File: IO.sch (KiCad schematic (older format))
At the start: 16 parts, among them U3 74AC541, U4 74LS138, U5 74HC245, U7 74LS148

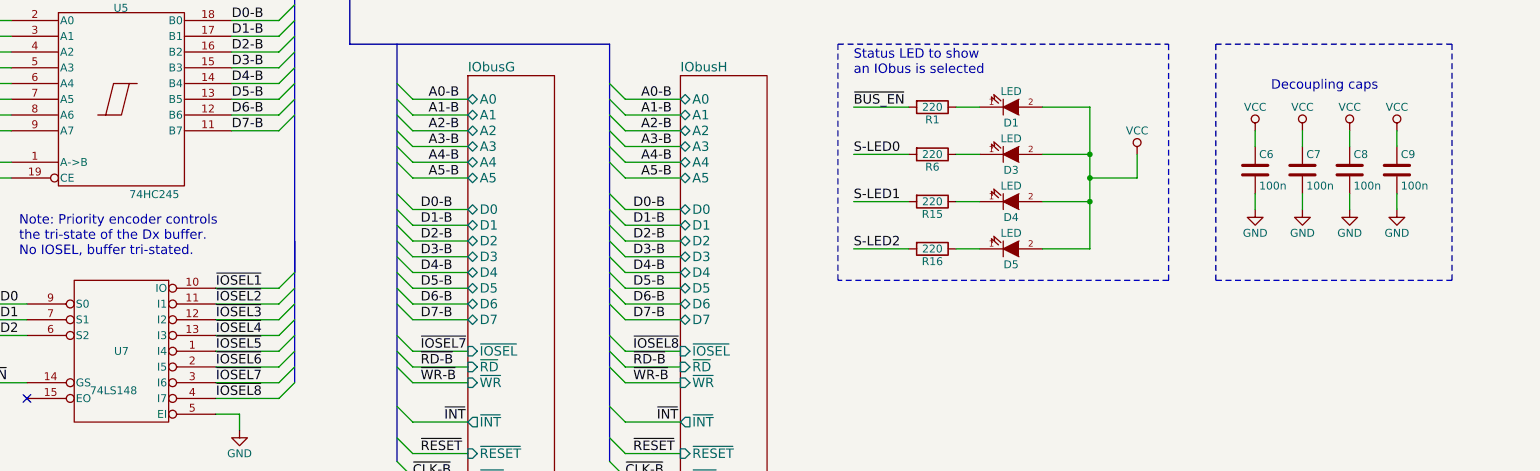
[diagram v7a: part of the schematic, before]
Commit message: Update PCB, better layout. Got Addr bus back in order
Think having both USB and DC input would be useful. Switchmode a plus
then plugpack/battery etc voltage doesn't matter. Plus I have a bag full
of those parts too!

I've refdes'd the linear reg just to deal with the net. Will remove if
we both are happy with switcher. Linear cheaper to kit out I guess.

Was trying to find a better way to combine USB and DC power rails than
just schottky diodes. If you have any ideas.

Going to have a big area under the IO ports, might be worth adding a USB
to serial, or sacrifice a IO port for some blinky LEDs and buttons?
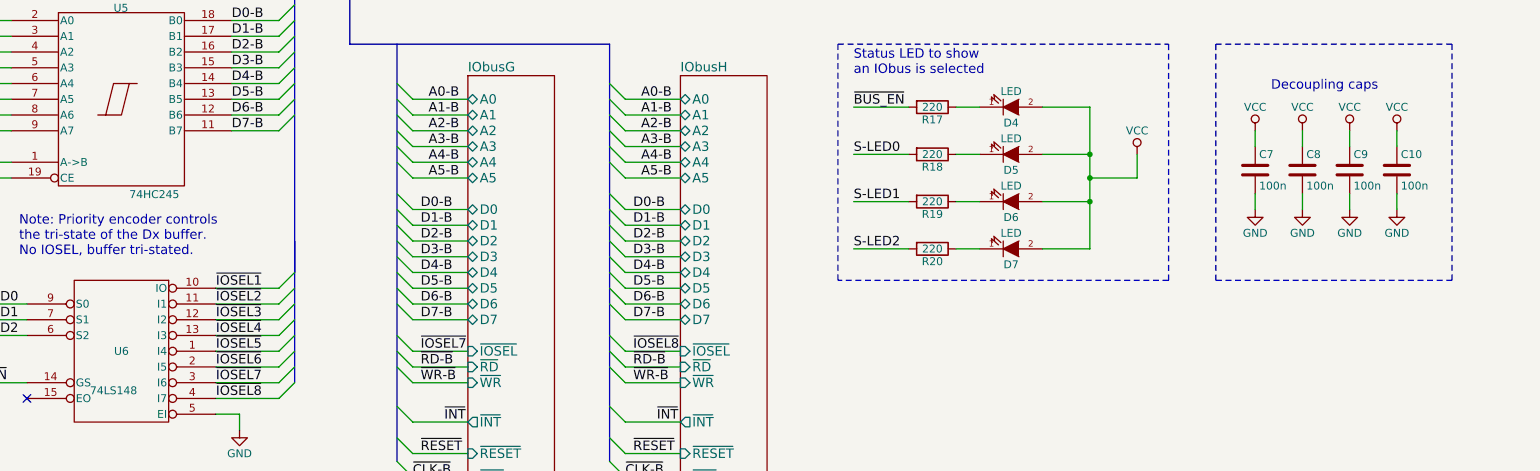
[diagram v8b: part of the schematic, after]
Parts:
- renumbered C9 to C10, C6 to C7, C7 to C8, C8 to C9, D1 to D4, D3 to D5, D4 to D6, D5 to D7, R1 to R17, R6 to R18, R15 to R19, R16 to R20, U7 to U6
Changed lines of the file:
@@
 $EndSheet
 $Comp
-L GND #PWR018
+L GND #PWR029
 U 1 1 5780EA7D
 P 1500 2000
-F 0 "#PWR018" H 1500 1750 50  0001 C CNN
+F 0 "#PWR029" H 1500 1750 50  0001 C CNN
 F 1 "GND" H 1500 1850 50  0000 C CNN
 F 2 "" H 1500 2000 50  0000 C CNN
@@
 	3250 3300 3350 3200
 $Comp
-L C C6
+L C C7
 U 1 1 57887A68
 P 9450 5150
-F 0 "C6" H 9475 5250 50  0000 L CNN
+F 0 "C7" H 9475 5250 50  0000 L CNN
 F 1 "100n" H 9475 5050 50  0000 L CNN
 F 2 "Capacitors_SMD:C_0805_HandSoldering" H 9488 5000 50  0001 C CNN
@@
 $EndComp
 $Comp
-L GND #PWR019
+L GND #PWR030
 U 1 1 57887A6E
 P 9450 5400
-F 0 "#PWR019" H 9450 5150 50  0001 C CNN
+F 0 "#PWR030" H 9450 5150 50  0001 C CNN
 F 1 "GND" H 9450 5250 50  0000 C CNN
 F 2 "" H 9450 5400 50  0000 C CNN
@@
 $EndComp
 $Comp
-L VCC #PWR020
+L VCC #PWR031
 U 1 1 57887A74
 P 9450 4900
-F 0 "#PWR020" H 9450 4750 50  0001 C CNN
+F 0 "#PWR031" H 9450 4750 50  0001 C CNN
 F 1 "VCC" H 9450 5050 50  0000 C CNN
 F 2 "" H 9450 4900 50  0000 C CNN
@@
 $EndComp
 $Comp
-L C C7
+L C C8
 U 1 1 57887A7C
 P 9750 5150
-F 0 "C7" H 9775 5250 50  0000 L CNN
+F 0 "C8" H 9775 5250 50  0000 L CNN
 F 1 "100n" H 9775 5050 50  0000 L CNN
 F 2 "Capacitors_SMD:C_0805_HandSoldering" H 9788 5000 50  0001 C CNN
@@
 $EndComp
 $Comp
-L GND #PWR021
+L GND #PWR032
 U 1 1 57887A82
 P 9750 5400
-F 0 "#PWR021" H 9750 5150 50  0001 C CNN
+F 0 "#PWR032" H 9750 5150 50  0001 C CNN
 F 1 "GND" H 9750 5250 50  0000 C CNN
 F 2 "" H 9750 5400 50  0000 C CNN
@@
 $EndComp
 $Comp
-L VCC #PWR022
+L VCC #PWR033
 U 1 1 57887A88
 P 9750 4900
-F 0 "#PWR022" H 9750 4750 50  0001 C CNN
+F 0 "#PWR033" H 9750 4750 50  0001 C CNN
 F 1 "VCC" H 9750 5050 50  0000 C CNN
 F 2 "" H 9750 4900 50  0000 C CNN
@@
 	3250 3800 3350 3700
 $Comp
-L C C8
+L C C9
 U 1 1 5785CC55
 P 10050 5150
-F 0 "C8" H 10075 5250 50  0000 L CNN
+F 0 "C9" H 10075 5250 50  0000 L CNN
 F 1 "100n" H 10075 5050 50  0000 L CNN
 F 2 "Capacitors_SMD:C_0805_HandSoldering" H 10088 5000 50  0001 C CNN
@@
 $EndComp
 $Comp
-L GND #PWR023
+L GND #PWR034
 U 1 1 5785CC5B
 P 10050 5400
-F 0 "#PWR023" H 10050 5150 50  0001 C CNN
+F 0 "#PWR034" H 10050 5150 50  0001 C CNN
 F 1 "GND" H 10050 5250 50  0000 C CNN
 F 2 "" H 10050 5400 50  0000 C CNN
@@
 $EndComp
 $Comp
-L VCC #PWR024
+L VCC #PWR035
 U 1 1 5785CC61
 P 10050 4900
-F 0 "#PWR024" H 10050 4750 50  0001 C CNN
+F 0 "#PWR035" H 10050 4750 50  0001 C CNN
 F 1 "VCC" H 10050 5050 50  0000 C CNN
 F 2 "" H 10050 4900 50  0000 C CNN
@@
 ~IOSEL8
 $Comp
-L C C9
+L C C10
 U 1 1 57897A03
 P 10350 5150
-F 0 "C9" H 10375 5250 50  0000 L CNN
+F 0 "C10" H 10375 5250 50  0000 L CNN
 F 1 "100n" H 10375 5050 50  0000 L CNN
 F 2 "Capacitors_SMD:C_0805_HandSoldering" H 10388 5000 50  0001 C CNN
@@
 $EndComp
 $Comp
-L GND #PWR025
+L GND #PWR036
 U 1 1 57897A09
 P 10350 5400
-F 0 "#PWR025" H 10350 5150 50  0001 C CNN
+F 0 "#PWR036" H 10350 5150 50  0001 C CNN
 F 1 "GND" H 10350 5250 50  0000 C CNN
 F 2 "" H 10350 5400 50  0000 C CNN
@@
 $EndComp
 $Comp
-L VCC #PWR026
+L VCC #PWR037
 U 1 1 57897A0F
 P 10350 4900
-F 0 "#PWR026" H 10350 4750 50  0001 C CNN
+F 0 "#PWR037" H 10350 4750 50  0001 C CNN
 F 1 "VCC" H 10350 5050 50  0000 C CNN
 F 2 "" H 10350 4900 50  0000 C CNN
@@
 ~RESET
 $Comp
-L 74LS148 U7
+L 74LS148 U6
 U 1 1 5790D09E
 P 2250 6300
-F 0 "U7" H 2250 6300 50  0000 C CNN
+F 0 "U6" H 2250 6300 50  0000 C CNN
 F 1 "74LS148" H 2300 6050 50  0000 C CNN
 F 2 "Housings_DIP:DIP-16_W7.62mm_LongPads" H 2250 6300 50  0001 C CNN
@@
 $EndComp
 $Comp
-L GND #PWR027
+L GND #PWR038
 U 1 1 5790EE64
 P 3000 6800
-F 0 "#PWR027" H 3000 6550 50  0001 C CNN
+F 0 "#PWR038" H 3000 6550 50  0001 C CNN
 F 1 "GND" H 3000 6650 50  0000 C CNN
 F 2 "" H 3000 6800 50  0000 C CNN
@@
 ~BUS_EN
 $Comp
-L R R1
+L R R17
 U 1 1 5792577C
 P 7400 4750
-F 0 "R1" V 7480 4750 50  0000 C CNN
+F 0 "R17" V 7480 4750 50  0000 C CNN
 F 1 "220" V 7400 4750 50  0000 C CNN
 F 2 "Resistors_SMD:R_0805_HandSoldering" H 7330 4750 50  0001 C CNN
@@
 $EndComp
 $Comp
-L R R6
+L R R18
 U 1 1 57925B76
 P 7400 5050
-F 0 "R6" V 7480 5050 50  0000 C CNN
+F 0 "R18" V 7480 5050 50  0000 C CNN
 F 1 "220" V 7400 5050 50  0000 C CNN
 F 2 "Resistors_SMD:R_0805_HandSoldering" H 7330 5050 50  0001 C CNN
@@
 $EndComp
 $Comp
-L R R15
+L R R19
 U 1 1 57925F63
 P 7400 5350
-F 0 "R15" V 7480 5350 50  0000 C CNN
+F 0 "R19" V 7480 5350 50  0000 C CNN
 F 1 "220" V 7400 5350 50  0000 C CNN
 F 2 "Resistors_SMD:R_0805_HandSoldering" H 7330 5350 50  0001 C CNN
@@
 $EndComp
 $Comp
-L R R16
+L R R20
 U 1 1 57926357
 P 7400 5650
-F 0 "R16" V 7480 5650 50  0000 C CNN
+F 0 "R20" V 7480 5650 50  0000 C CNN
 F 1 "220" V 7400 5650 50  0000 C CNN
 F 2 "Resistors_SMD:R_0805_HandSoldering" H 7330 5650 50  0001 C CNN
@@
 $EndComp
 $Comp
-L LED D1
+L LED D4
 U 1 1 57926740
 P 7900 4750
-F 0 "D1" H 7900 4850 50  0000 C CNN
+F 0 "D4" H 7900 4850 50  0000 C CNN
 F 1 "LED" H 7900 4650 50  0000 C CNN
 F 2 "LEDs:LED_1206" H 7900 4750 50  0001 C CNN
@@
 $EndComp
 $Comp
-L LED D3
+L LED D5
 U 1 1 57926B42
 P 7900 5050
-F 0 "D3" H 7900 5150 50  0000 C CNN
+F 0 "D5" H 7900 5150 50  0000 C CNN
 F 1 "LED" H 7900 4950 50  0000 C CNN
 F 2 "LEDs:LED_1206" H 7900 5050 50  0001 C CNN
@@
 $EndComp
 $Comp
-L LED D4
+L LED D6
 U 1 1 57926F3A
 P 7900 5350
-F 0 "D4" H 7900 5450 50  0000 C CNN
+F 0 "D6" H 7900 5450 50  0000 C CNN
 F 1 "LED" H 7900 5250 50  0000 C CNN
 F 2 "LEDs:LED_1206" H 7900 5350 50  0001 C CNN
@@
 $EndComp
 $Comp
-L LED D5
+L LED D7
 U 1 1 57927335
 P 7900 5650
-F 0 "D5" H 7900 5750 50  0000 C CNN
+F 0 "D7" H 7900 5750 50  0000 C CNN
 F 1 "LED" H 7900 5550 50  0000 C CNN
 F 2 "LEDs:LED_1206" H 7900 5650 50  0001 C CNN
@@
 $EndComp
 $Comp
-L VCC #PWR028
+L VCC #PWR039
 U 1 1 5792ACFD
 P 8700 5050
-F 0 "#PWR028" H 8700 4900 50  0001 C CNN
+F 0 "#PWR039" H 8700 4900 50  0001 C CNN
 F 1 "VCC" H 8700 5200 50  0000 C CNN
 F 2 "" H 8700 5050 50  0000 C CNN
@@
 	1450 3200 1650 3200
 $Comp
-L GND #PWR029
+L GND #PWR040
 U 1 1 579690D1
 P 1600 3350
-F 0 "#PWR029" H 1600 3100 50  0001 C CNN
+F 0 "#PWR040" H 1600 3100 50  0001 C CNN
 F 1 "GND" H 1600 3200 50  0000 C CNN
 F 2 "" H 1600 3350 50  0000 C CNN
